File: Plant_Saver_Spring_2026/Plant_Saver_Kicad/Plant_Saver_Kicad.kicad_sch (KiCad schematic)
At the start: 25 parts, among them Q9 G09P02L, SW1 Select, SW2 Select, SW3 Up, SW4 Down, SW5 Change Screen, SW6 Select, SW8 NK236WH, U1 CDBA140SL-HF, U2 CDBA140SL-HF, U3 CDBA140SL-HF, U4 CDBA140SL-HF, U5 ESP32-WROOM-32E-N16, U8 ESP32-WROOM-32D

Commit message: Found NTC Thermistor
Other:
- note added: "This is Dumb, Replace w/ NMOS on negative side"
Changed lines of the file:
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@@
+		)
+	)
+	(text "This is Dumb, Replace w/ NMOS on negative side"
+		(exclude_from_sim no)
+		(at 260.604 168.148 0)
+		(effects
+			(font
+				(size 1.27 1.27)
+			)
 		)
 	)

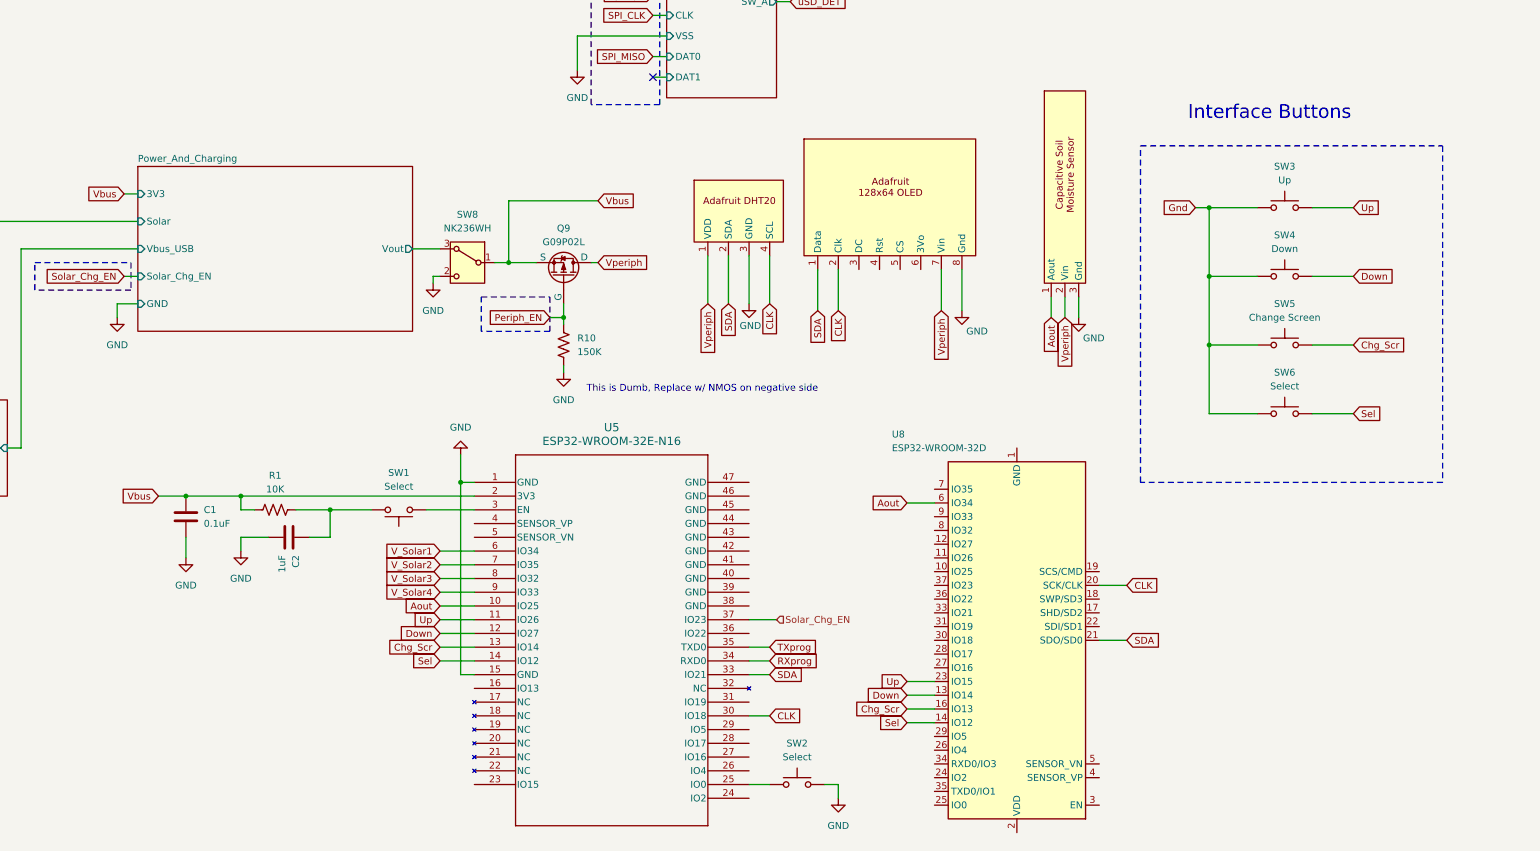
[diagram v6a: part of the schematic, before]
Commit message: StripBoardAddon
Instead of making a whole different sketch I used a hierarch so the pins match with the ones on the esp32. It's got the 4 pushbuttons and 3 LED's. I could not find where the LED's are supposed to be so right now they are just pins tied to ground. The error LED pin is also left untied because I am unsure what pin to tie it to.
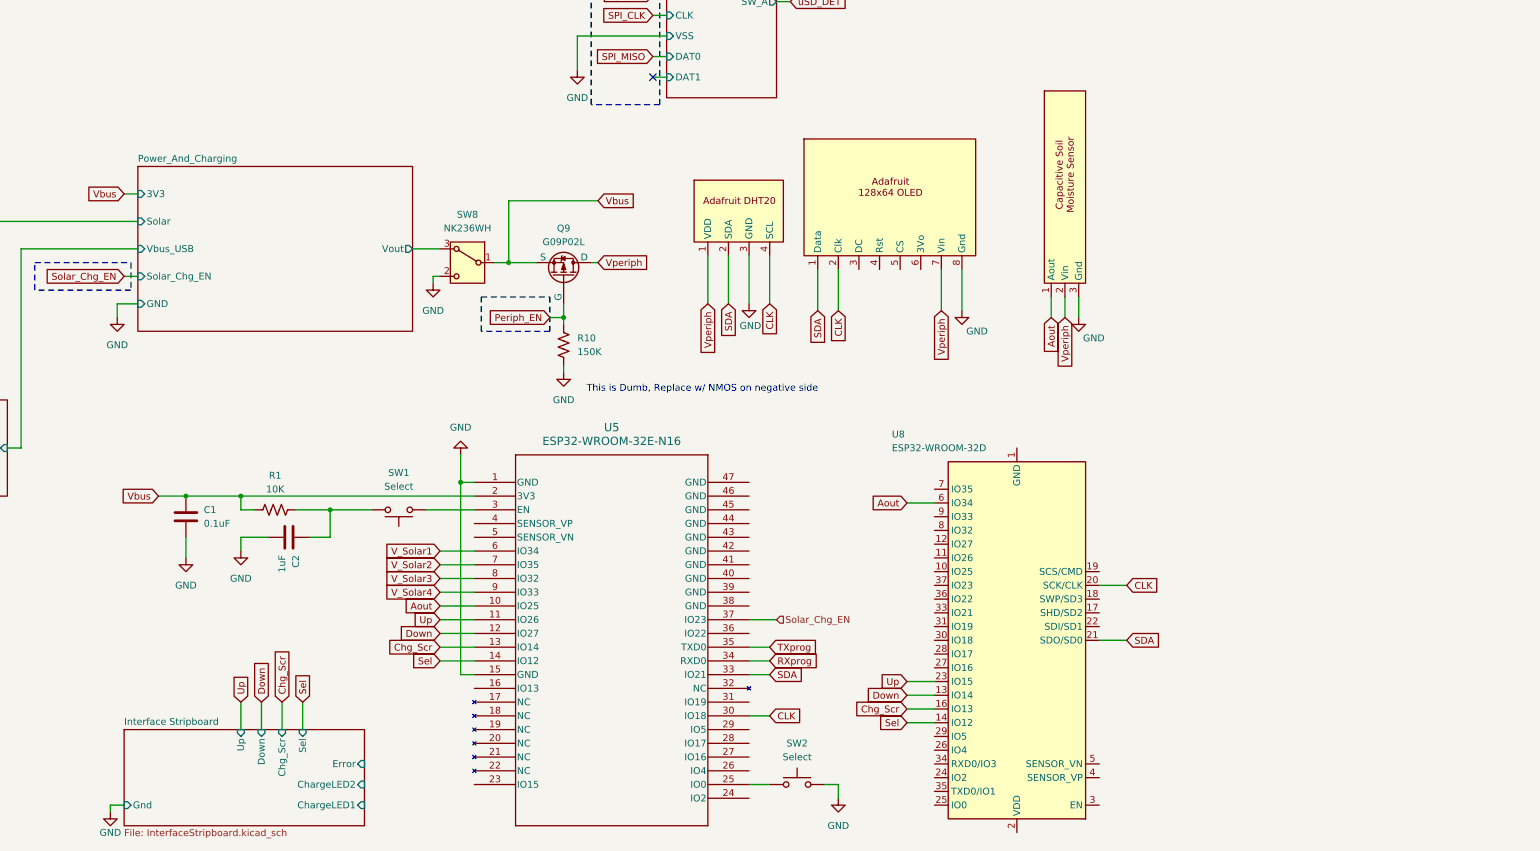
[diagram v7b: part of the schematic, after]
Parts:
- removed SW3: Up, symbol Switch:SW_Push
- removed SW4: Down, symbol Switch:SW_Push
- removed SW5: Change Screen, symbol Switch:SW_Push
- removed SW6: Select, symbol Switch:SW_Push
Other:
- added sheet Interface Stripboard (InterfaceStripboard.kicad_sch)
- note removed: "Interface Buttons"

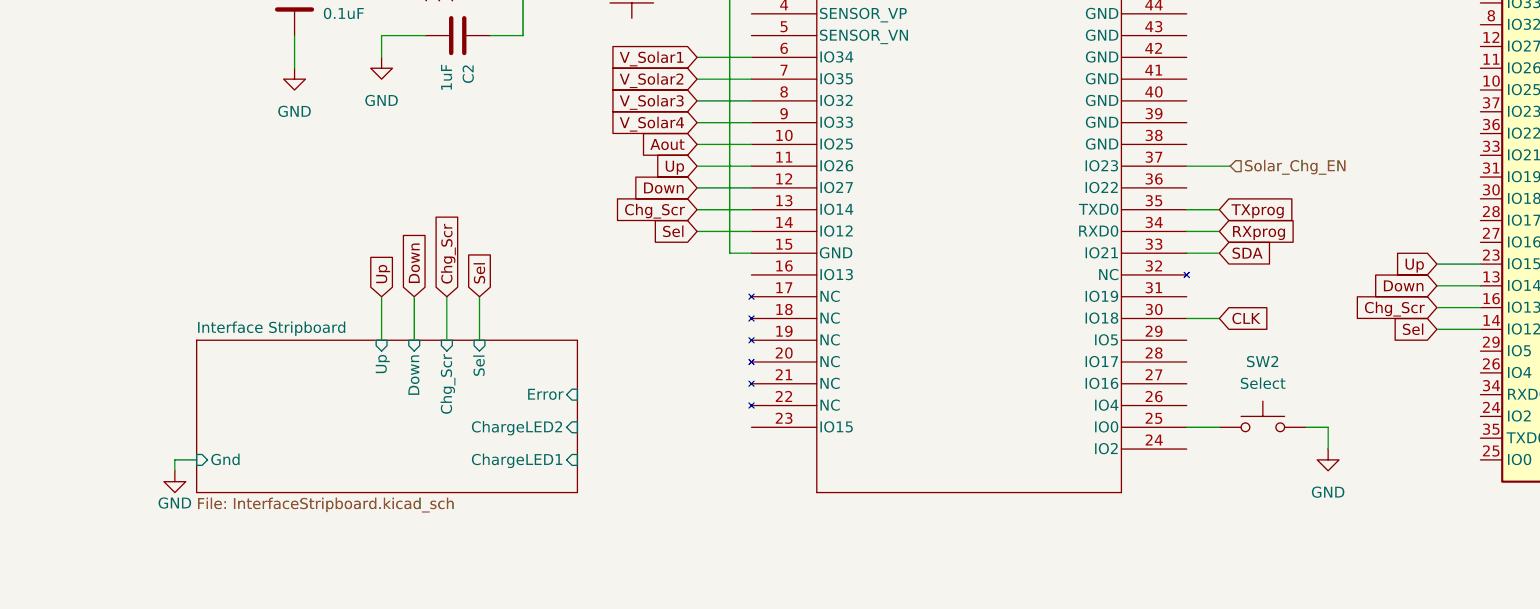
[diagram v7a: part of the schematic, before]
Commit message: StripBoardTouchUp
Made everything on the stripboard go into connector pins that then integrate into the main sketch. Made Error LED go into pin 26 on the esp32.
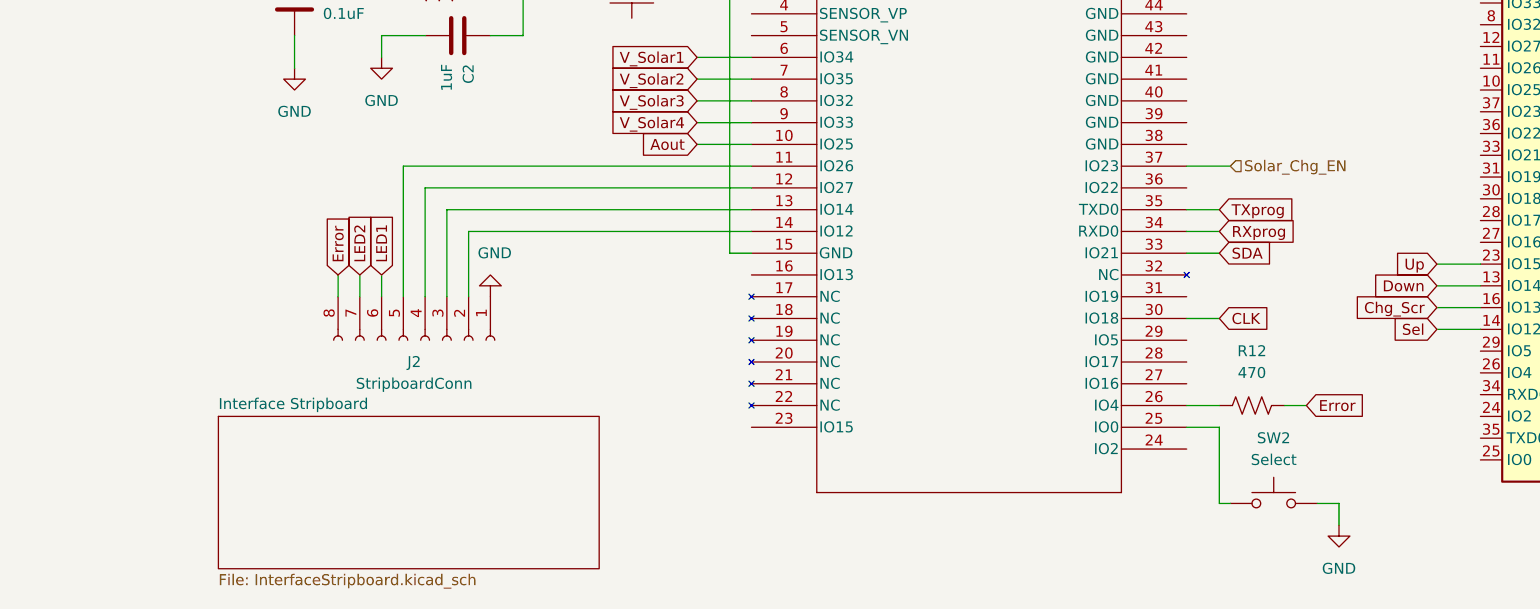
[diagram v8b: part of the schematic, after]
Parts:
- added J2: StripboardConn, symbol Connector:Conn_01x08_Socket
- added R12: 470, Resistor_THT:R_Axial_DIN0207_L6.3mm_D2.5mm_P10.16mm_Horizontal, symbol Device:R_US
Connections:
- net Chg_Scr: no longer U5.13 (IO14)
- net Down: no longer U5.12 (IO27)
- net GND: now also J2.1 (Pin_1)
- net Sel: no longer U5.14 (IO12)
- net Up: no longer U5.11 (IO26)
- net at U5.26 (IO4): now also R12.1
- new net: J2.5 (Pin_5), U5.11 (IO26)
- new net: J2.4 (Pin_4), U5.12 (IO27)
- new net: J2.3 (Pin_3), U5.13 (IO14)
- new net: J2.2 (Pin_2), U5.14 (IO12)
- new net Error: J2.8 (Pin_8), R12.2
- new net LED1: J2.6 (Pin_6)
- new net LED2: J2.7 (Pin_7)
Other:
- sheet Interface Stripboard ports: added none; removed ChargeLED1, ChargeLED2, Chg_Scr, Down, Error, Gnd, Sel, Up
- moved on the sheet: SW2
